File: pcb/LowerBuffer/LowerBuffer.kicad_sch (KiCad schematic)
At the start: 58 parts, among them J1 AudioJack3, J2 AudioJack3, J3 Barrel_Jack, J4 Conn_01x04, Q1 AO3401A, U1 TL072

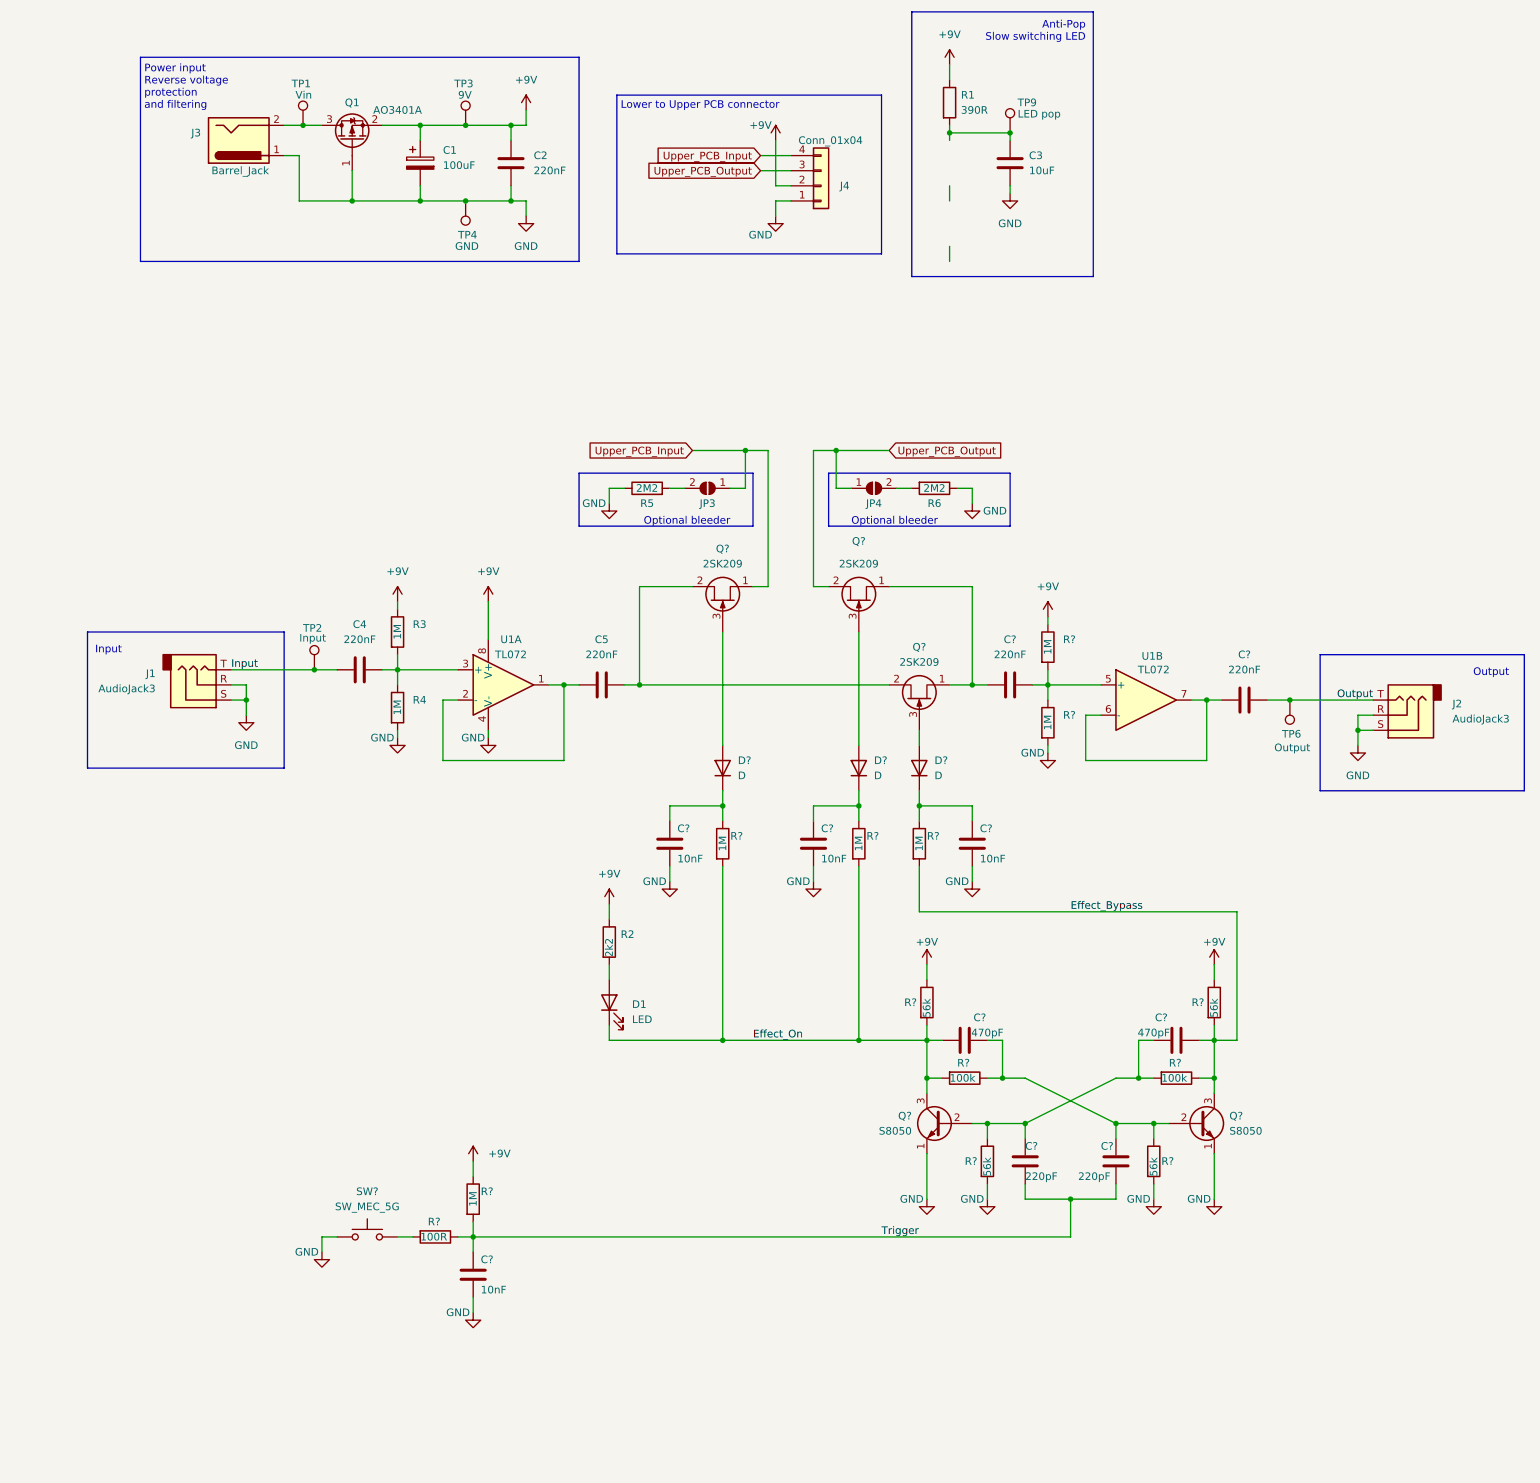
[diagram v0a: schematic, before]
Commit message: [LowerBuffer] Minor schematic cleanup
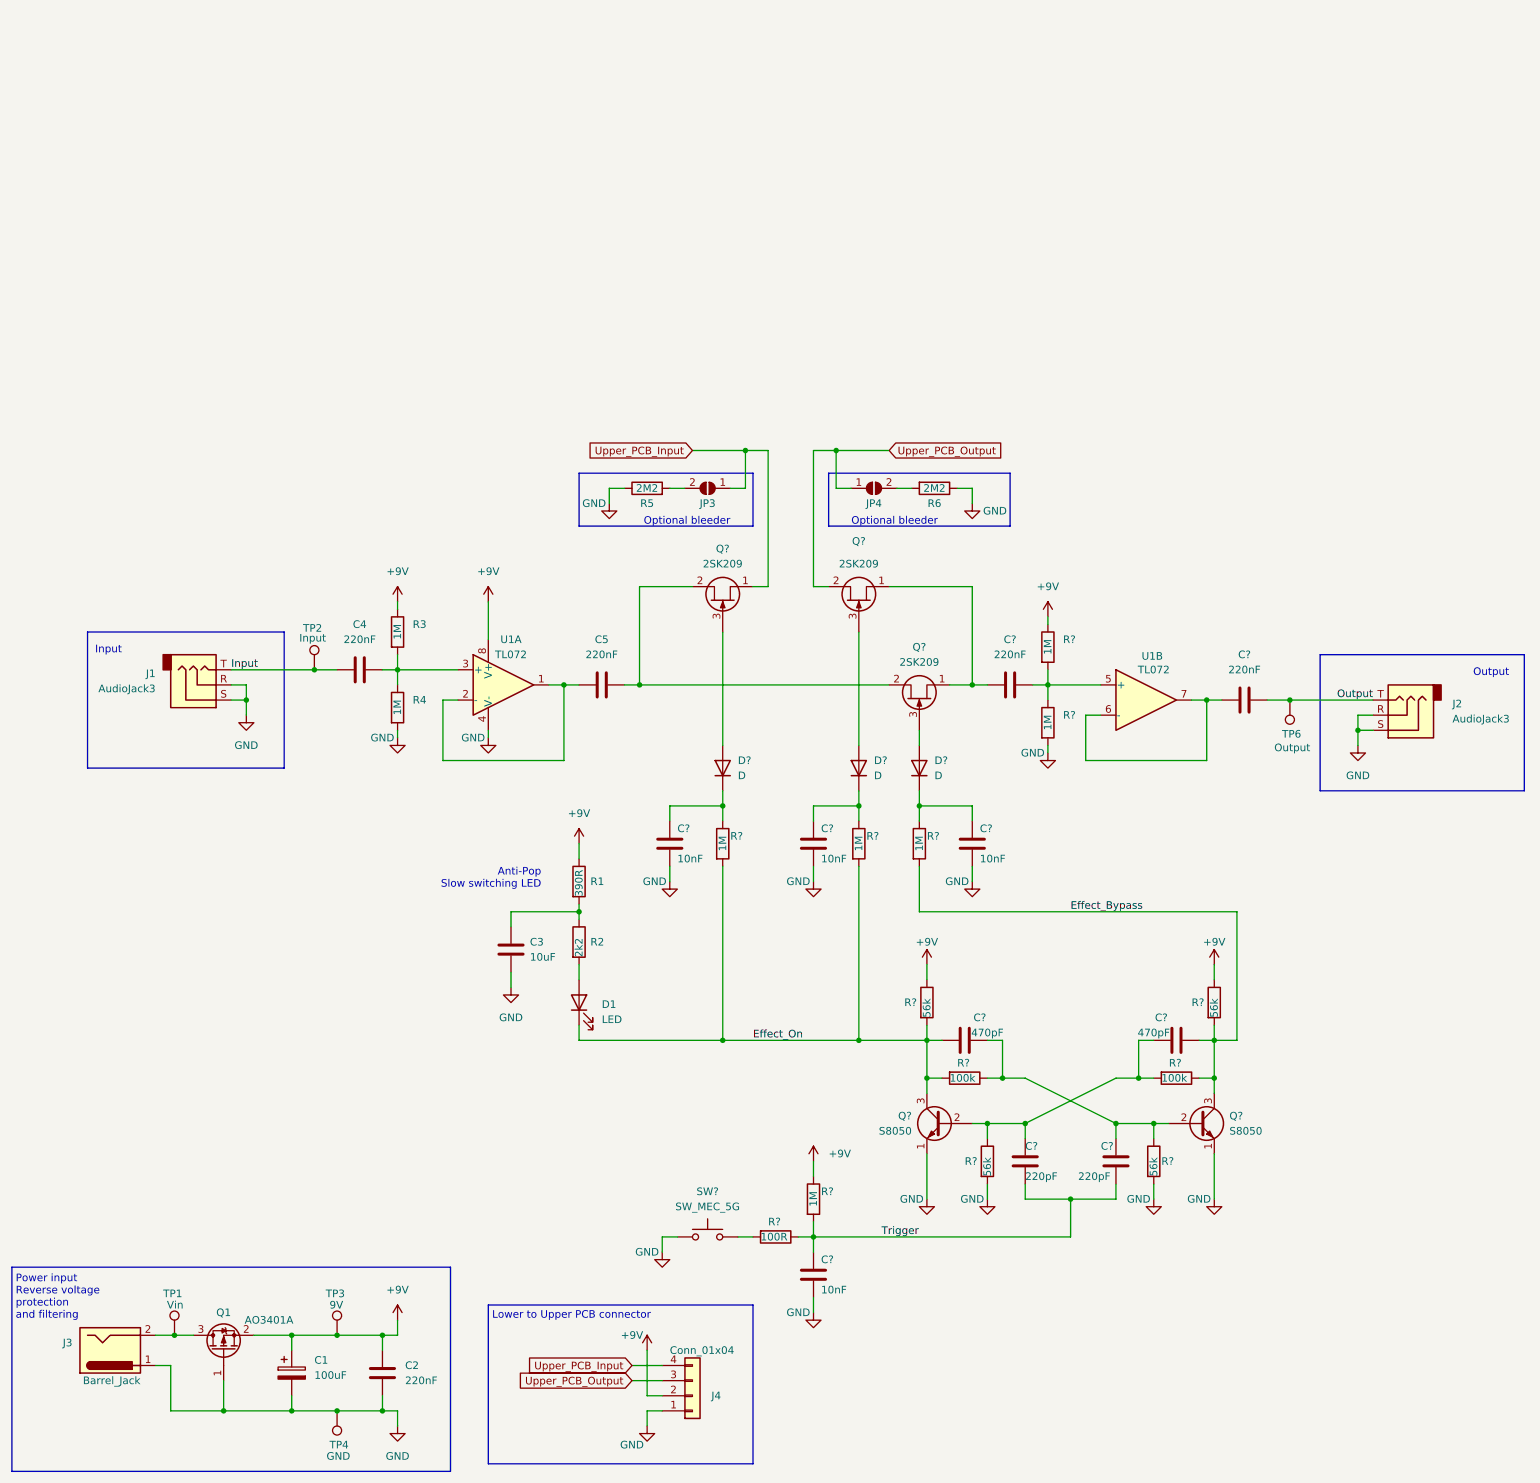
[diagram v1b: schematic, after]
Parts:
- removed TP9: LED pop, TestPoint:TestPoint_Pad_D2.0mm, symbol Connector:TestPoint
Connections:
- net +9V: no longer R2.1
- net at C3.1, R1.2: now also R2.1
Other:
- moved on the sheet: C1, C2, C3, C?, D1, J3, J4, Q1, R1, R2, R?, SW?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
